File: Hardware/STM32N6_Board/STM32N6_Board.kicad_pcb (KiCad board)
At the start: 2 copper layers, 1 x 0.7 mm, 141 parts, among them J1 Conn_01x02_Pin, J10 BOOT0, J11 Conn_01x18_Socket, J12 Conn_01x18_Socket, J2 Conn_01x02_Pin, J3 Conn_01x08_Pin, J4 Conn_01x18_Pin, J5 Conn_01x18_Pin, J6 Conn_01x05_Pin, J7 SFW15R-2STE1LF, J8 12401832E402A, J9 BOOT1, SW2 SW_Push, U1 STM32N657I0H3Q, U10 STMPS2151STR, U11 IS42S16800F-7BL, U12 ECMF2-40A100N6, U13 ECMF2-40A100N6, U14 ECMF2-40A100N6, U2 SPX5205-ADJ, U3 SPX5205-ADJ, U4 SPX5205-ADJ, U5 SPX5205-ADJ, U6 MC34064-ADJ-TR, U7 MX25LM51245GXDI00, U8 SPX5205-ADJ, U9 ECMF2-40A100N6, Y1 32.768kHz, Y3 48MHz

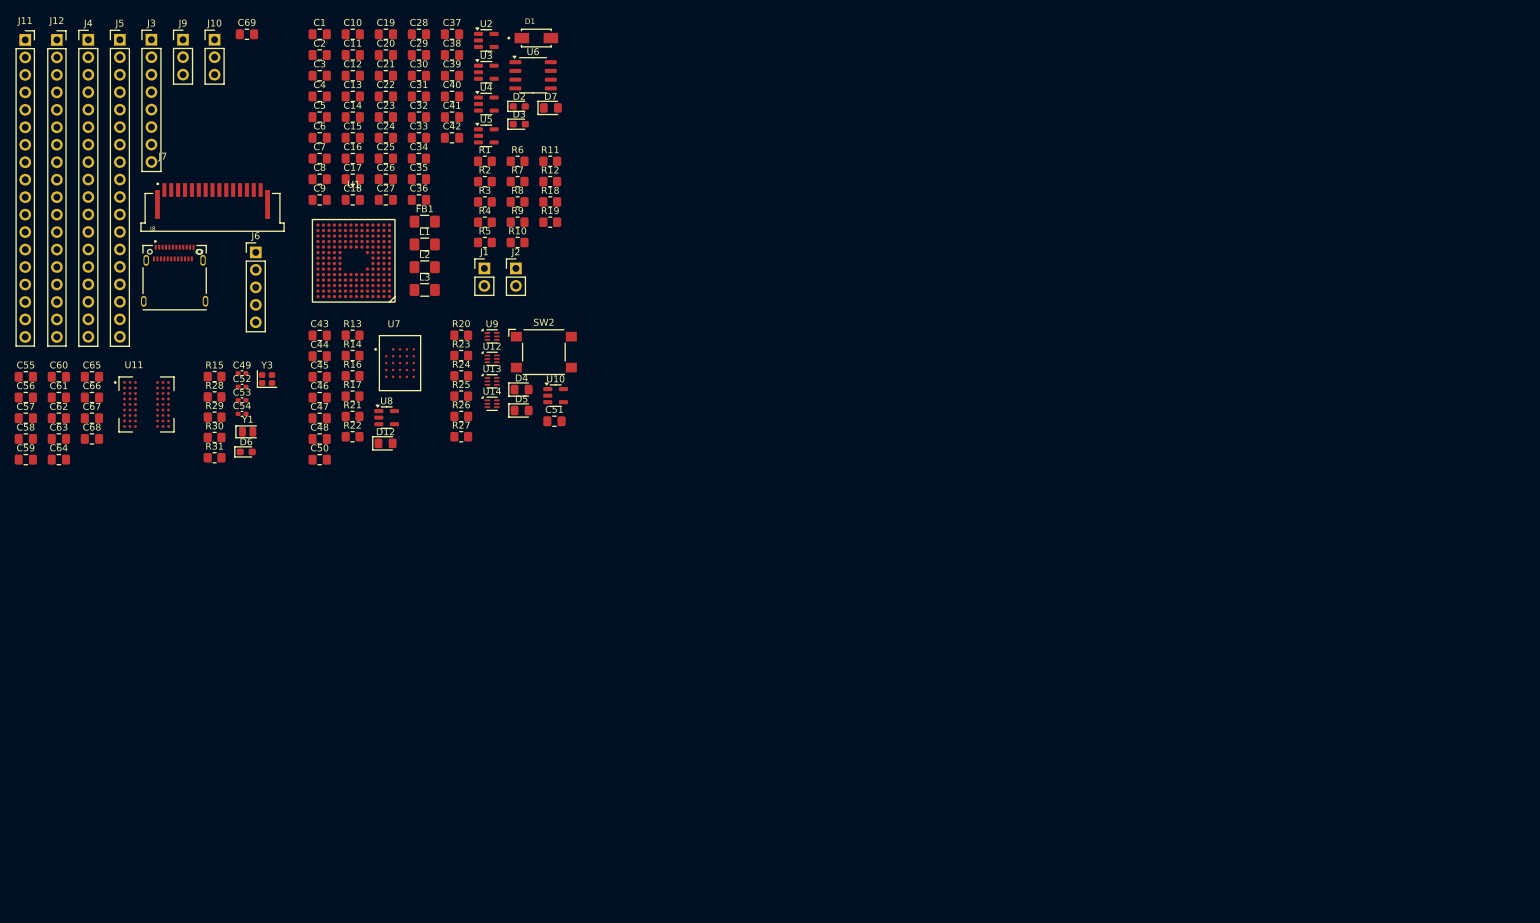
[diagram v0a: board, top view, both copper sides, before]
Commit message: Completed a lot of the layout of the STM Board
- Major layout complete, but all the wiring still left. 488 open nets!
- The STM32's BGA fanout is complete, now comes laying out traces
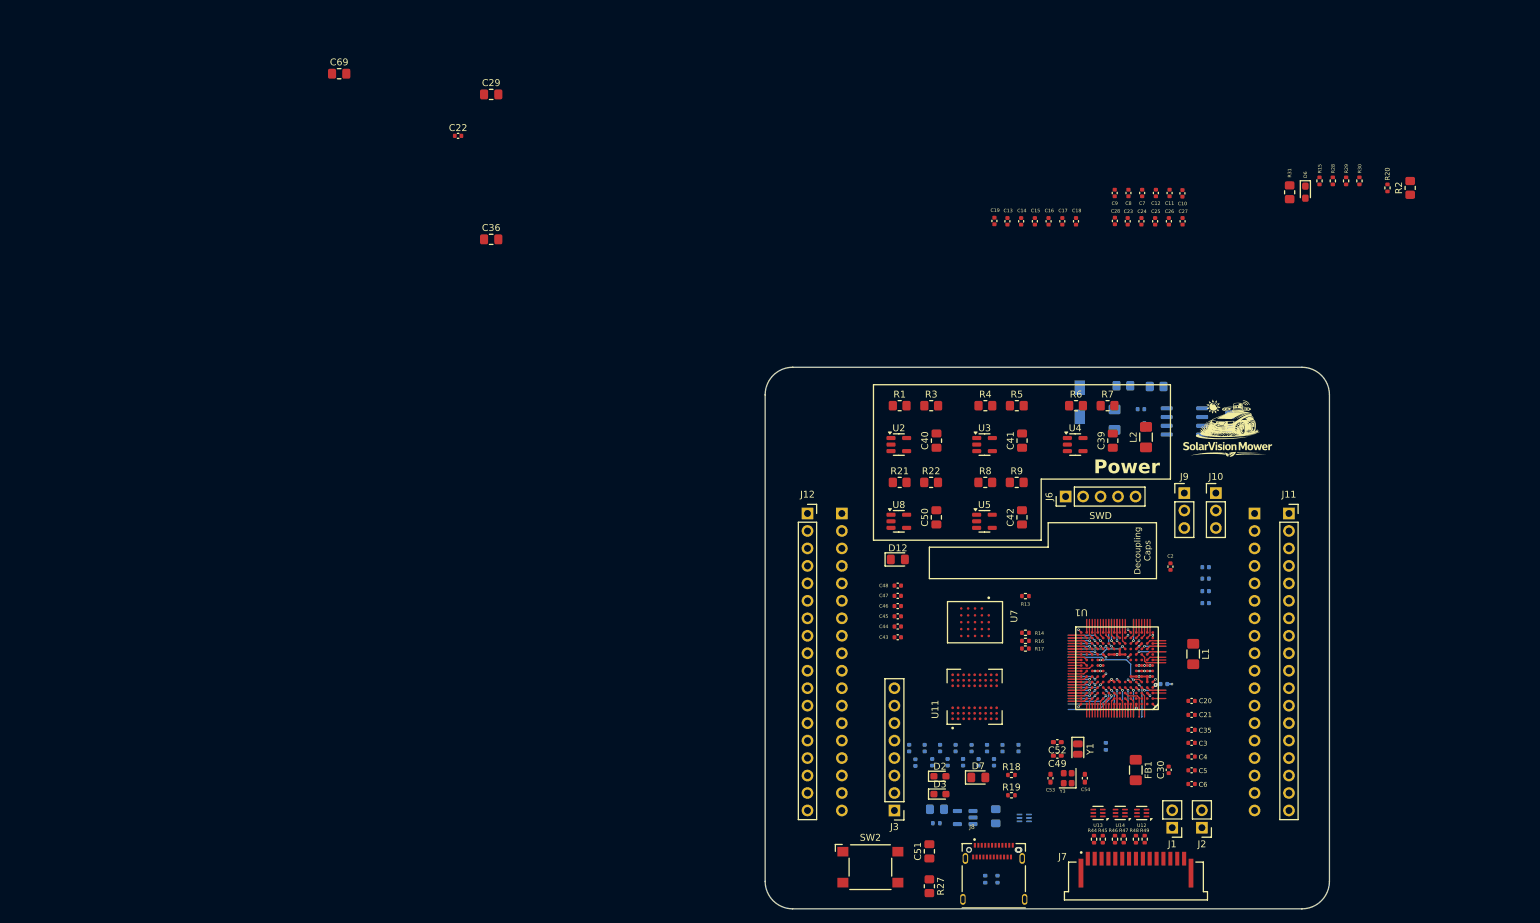
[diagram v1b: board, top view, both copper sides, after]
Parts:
- added G***: LOGO, STM32N6_Footprints:SolarVisionMowerLogo, F.Cu at (216.2, 87.6)
- added R44: 0R, Resistor_SMD:R_0402_1005Metric, F.Cu at (196.7, 147.4)
- added R45: 0R, Resistor_SMD:R_0402_1005Metric, F.Cu at (197.9, 147.4)
- added R46: 0R, Resistor_SMD:R_0402_1005Metric, F.Cu at (199.7, 147.4)
- added R47: 0R, Resistor_SMD:R_0402_1005Metric, F.Cu at (201.0, 147.3)
- added R48: 0R, Resistor_SMD:R_0402_1005Metric, F.Cu at (202.8, 147.4)
- added R49: 0R, Resistor_SMD:R_0402_1005Metric, F.Cu at (204.0, 147.3)
- C1, C31, C32, C33, C34, C37, C38, C55, C56, C57, C58, C59, C60, C61, C62, C63, C64, C65, C66, C67, C68: footprint Capacitor_SMD:C_0805_2012Metric_Pad1.18x1.45mm_HandSolder -> Capacitor_SMD:C_0402_1005Metric; moved to B.Cu
- C10, C11, C12, C13, C14, C15, C16, C17, C18, C19, C2, C20, C21, C22, C23, C24, C25, C26, C27, C28, C3, C30, C35, C4, C43, C44, C45, C46, C47, C48, C5, C6, C7, C8, C9: footprint Capacitor_SMD:C_0805_2012Metric_Pad1.18x1.45mm_HandSolder -> Capacitor_SMD:C_0402_1005Metric
- D1, D4, D5, J4, J5, L3, R10, R11, R12, U10, U6, U9: moved to B.Cu
- R13, R14, R15, R16, R17, R18, R19, R20, R28, R29, R30: footprint Resistor_SMD:R_0805_2012Metric_Pad1.20x1.40mm_HandSolder -> Resistor_SMD:R_0402_1005Metric
- R23, R24, R25, R26: footprint Resistor_SMD:R_0805_2012Metric_Pad1.20x1.40mm_HandSolder -> Resistor_SMD:R_0402_1005Metric; moved to B.Cu
- moved J11 196.2 mm to (225.0, 100.0)
- moved J4 183.0 mm to (220.0, 100.0), turned to 180 degrees
- moved R30 170.6 mm to (235.2, 51.6), turned to 90 degrees
- moved R29 168.1 mm to (233.3, 51.6), turned to 90 degrees
- moved J7 165.8 mm to (202.8, 152.3)
- moved R28 165.6 mm to (231.4, 51.6), turned to 90 degrees
- moved R15 163.1 mm to (229.4, 51.6), turned to 90 degrees
- moved R31 161.0 mm to (225.1, 53.3), turned to -90 degrees
- moved J10 159.8 mm to (214.4, 97.0)
- moved J9 159.8 mm to (209.8, 97.0)
- moved C3 159.6 mm to (210.8, 133.3)
- moved C4 159.0 mm to (210.8, 135.3)
- moved D6 158.6 mm to (227.4, 53.3), turned to -90 degrees
- moved C5 158.4 mm to (210.8, 137.3)
- moved C6 157.8 mm to (210.8, 139.3)
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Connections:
- net Net-(U6-DRC) renamed /Power_Unit/Buck_Feedback
- C35 pad 2: /Power_Unit/VFBSMPS -> GND
- J7 pad 2: /Analog_Unit/D0N -> Net-(J7-Pad2)
- J7 pad 3: /Analog_Unit/D0P -> Net-(J7-Pad3)
- J7 pad 5: /Analog_Unit/D1N -> Net-(J7-Pad5)
- J7 pad 6: /Analog_Unit/D1P -> Net-(J7-Pad6)
- J7 pad 8: /Analog_Unit/CKN -> Net-(J7-Pad8)
- J7 pad 9: /Analog_Unit/CKP -> Net-(J7-Pad9)
- U1 pad N11: /Analog_Unit/EN -> /Analog_Unit/EN_USB
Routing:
- net /Analog_Unit/PWR_ON: track 0.00 -> 13.4 mm, vias 0 -> 1
- net GND: track 0.00 -> 10.3 mm, vias 0 -> 12
- net /FMC_SDRAM/FMC_D0: track 0.00 -> 8.96 mm, vias 0 -> 1
- net /FMC_SDRAM/FMC_SDNRAS: track 0.00 -> 8.04 mm, vias 0 -> 1
- net /FMC_SDRAM/FMC_SDNE0: track 0.00 -> 7.82 mm, vias 0 -> 1
- net /FMC_SDRAM/FMC_SKNCAS: track 0.00 -> 6.40 mm, vias 0 -> 1
- net /FMC_SDRAM/FMC_D6: track 0.00 -> 6.24 mm, vias 0 -> 1
- net /FMC_SDRAM/FMC_D9: track 0.00 -> 5.60 mm, vias 0 -> 1
- net /Analog_Unit/NRST: track 0.00 -> 5.45 mm, vias 0 -> 1
- net /FMC_SDRAM/FMC_A0: track 0.00 -> 5.43 mm, vias 0 -> 1
- net /Connectors/HDP0: track 0.00 -> 5.13 mm
- net /FMC_SDRAM/FMC_A5: track 0.00 -> 4.63 mm, vias 0 -> 1
- net /FMC_SDRAM/FMC_A3: track 0.00 -> 4.63 mm, vias 0 -> 1
- net /Connectors/SPI1_MOSI: track 0.00 -> 4.63 mm, vias 0 -> 1
- net /FMC_SDRAM/FMC_A4: track 0.00 -> 4.63 mm, vias 0 -> 1
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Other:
- board size 1 x 0.7 mm -> 82 x 78.7 mm
- copper layers 2 -> 4
- board text added: "Decoupling Caps"
- board text added: "Power"
- board text added: "SWD"

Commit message: Added bypass capacitors to the STM32
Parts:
- C10, C11, C12, C13, C14, C15, C16, C17, C18, C19, C23, C24, C25, C26, C27, C28, C3, C35, C4, C5, C6, C7, C8, C9: moved to B.Cu
- R2: footprint Resistor_SMD:R_0805_2012Metric_Pad1.20x1.40mm_HandSolder -> Resistor_SMD:R_0402_1005Metric
- moved R2 72.7 mm to (213.7, 119.4), turned to -90 degrees
- moved C9 70.0 mm to (207.5, 122.9)
- moved C12 69.7 mm to (210.6, 122.9)
- moved C8 69.7 mm to (206.5, 122.9)
- moved C11 69.6 mm to (209.6, 122.9)
- moved C7 69.6 mm to (205.5, 122.9)
- moved C10 69.5 mm to (208.5, 122.9)
- moved C17 68.0 mm to (200.7, 125.0), turned to 0 degrees
- moved C18 67.6 mm to (198.7, 125.0), turned to 180 degrees
- moved C19 67.3 mm to (198.9, 122.7), turned to -90 degrees
- moved C13 67.0 mm to (199.9, 122.7), turned to -90 degrees
- moved C14 65.3 mm to (196.8, 121.9)
- moved C15 64.9 mm to (195.8, 121.9)
- moved C16 64.6 mm to (194.8, 121.9)
- moved C28 62.3 mm to (202.4, 119.7)
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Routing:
- net GND: track 10.3 -> 39.4 mm, vias 12 -> 21
- net /Power_Unit/VFBSMPS: track 2.87 -> 14.8 mm, vias 0 -> 1
- net /Power_Unit/VLXSMPS: track 2.40 -> 14.2 mm
- net VDD: track 4.10 -> 11.7 mm
- net /Power_Unit/VDDCORE: track 3.77 -> 11.2 mm
- net /Power_Unit/VDDSMPS: track 2.40 -> 8.31 mm, vias 3 -> 5
- net /Power_Unit/VREFP: track 1.90 -> 7.38 mm
- net /Connectors/USART3_RX: track 3.67 -> 8.67 mm
- net /Connectors/SPI1_MISO: track 4.63 -> 9.63 mm
- net /Connectors/I2C1_SCL: track 4.63 -> 9.63 mm
- net /Connectors/USART3_TX: track 2.87 -> 7.87 mm
- net /Connectors/USART2_TX: track 1.90 -> 6.90 mm
- net /Connectors/USART2_RX: track 2.87 -> 7.87 mm
- net /Connectors/USART1_TX: track 2.87 -> 7.87 mm
- net /Connectors/USART1_RX: track 3.67 -> 8.67 mm
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- added copper zone on In2.Cu, net +5V
- added copper zone on In1.Cu, net GND
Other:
- board text removed: "Decoupling Caps"

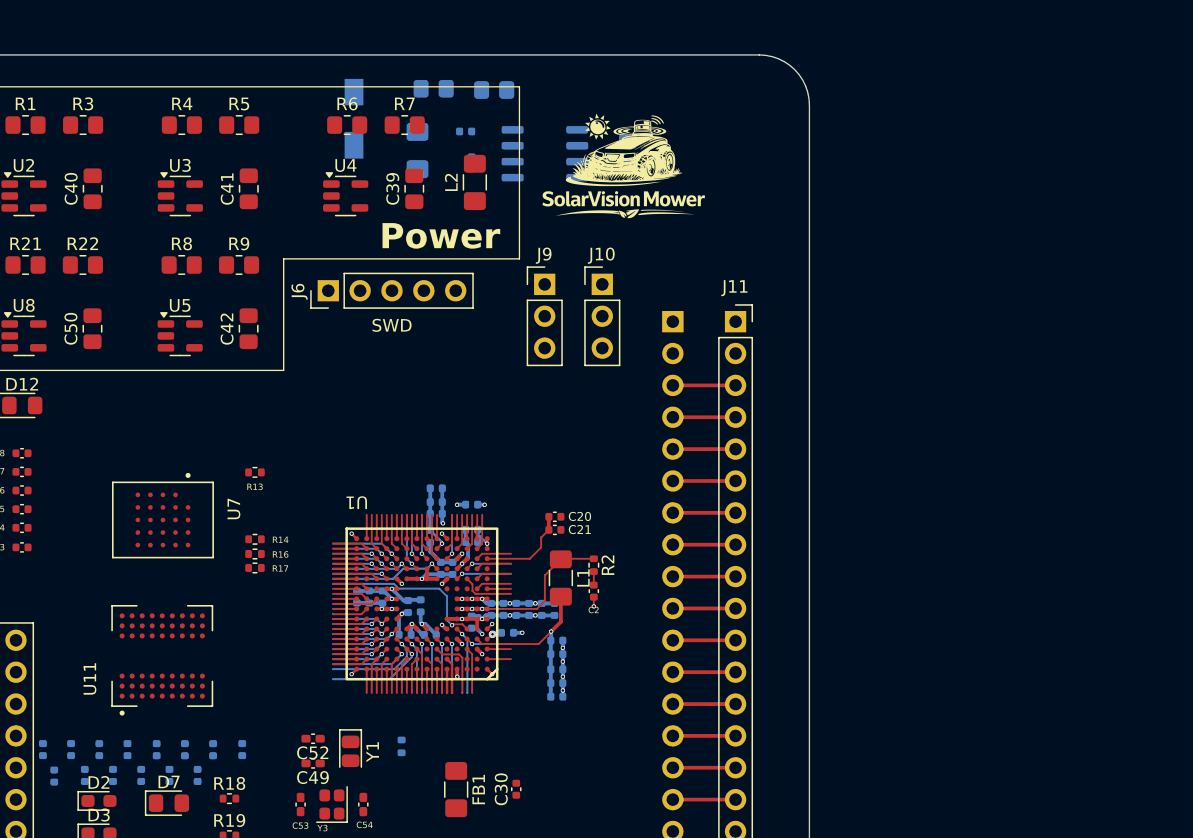
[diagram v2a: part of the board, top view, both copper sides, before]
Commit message: Completed SDRAM bga fanout
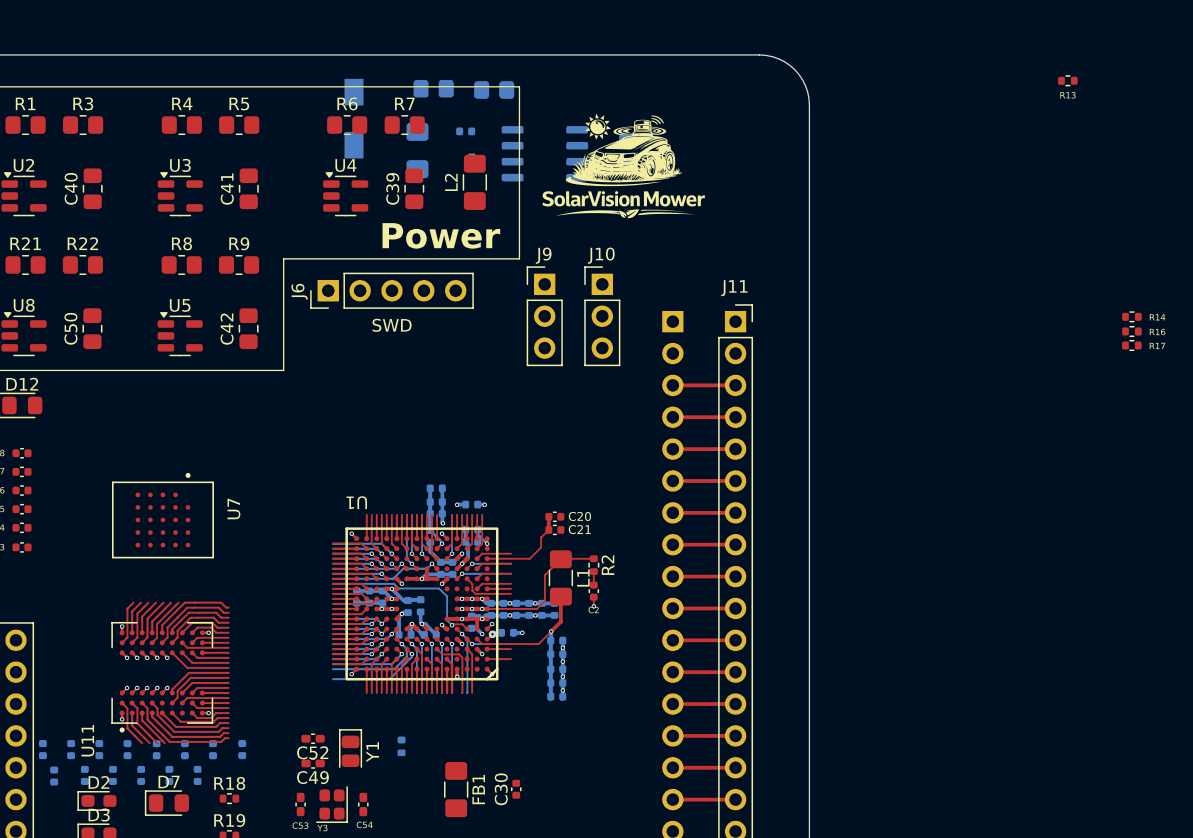
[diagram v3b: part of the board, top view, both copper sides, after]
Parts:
- moved R14 72.1 mm to (256.6, 99.6)
- moved R16 72.1 mm to (256.6, 100.8)
- moved R17 72.1 mm to (256.6, 101.9)
- moved R13 71.9 mm to (251.5, 80.8)
- moved U11 1.35 mm to (179.3, 128.0)
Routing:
- net /FMC_SDRAM/FMC_D11: track 1.90 -> 10.7 mm
- net /FMC_SDRAM/FMC_D9: track 5.60 -> 13.1 mm
- net /FMC_SDRAM/FMC_D10: track 2.87 -> 10.1 mm
- net /FMC_SDRAM/FMC_NBL0: track 2.87 -> 9.96 mm
- net /FMC_SDRAM/FMC_D7: track 1.90 -> 8.71 mm
- net /FMC_SDRAM/FMC_D8: track 4.63 -> 10.5 mm
- net /FMC_SDRAM/FMC_SDNRAS: track 8.04 -> 13.8 mm
- net /FMC_SDRAM/FMC_SDCLK: track 3.67 -> 9.31 mm
- net /FMC_SDRAM/FMC_SDNWE: track 2.87 -> 8.36 mm
- net /FMC_SDRAM/FMC_SDCKE0: track 2.87 -> 8.19 mm
- net /FMC_SDRAM/FMC_SKNCAS: track 6.40 -> 11.4 mm
- net /FMC_SDRAM/FMC_NBL1: track 3.67 -> 8.57 mm
- net /FMC_SDRAM/FMC_SDNE0: track 7.82 -> 12.0 mm
- net /FMC_SDRAM/FMC_D6: track 6.24 -> 10.3 mm
- net /FMC_SDRAM/FMC_BA0: track 1.90 -> 5.93 mm
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
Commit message: Completed the IS42S SDRAM routing. Lord have mercy
- Routing is complete (somewhat)
- Spacing between traces is 0.5mm, address and data lines 0.1565mm wide
- 0.1565mm should maintain ~50 Ohms impedance.
- STILL NEED TO DO:
  - Length matching. Datasheet + STM App Note says +-10mm
  - 10nF stitching caps along vias, for return currents
- Remind me to *never* use a 4-layer board for something like this
  again. D:
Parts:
- moved C59 66.5 mm to (246.4, 119.3)
- moved C66 66.5 mm to (247.7, 117.2)
- moved C57 66.5 mm to (242.0, 119.3)
- moved C58 66.5 mm to (244.2, 119.3)
- moved C67 66.5 mm to (245.4, 117.2)
- moved C68 66.5 mm to (243.2, 117.2)
- moved C49 60.5 mm to (251.8, 134.1)
- moved C52 60.5 mm to (251.8, 132.1)
- moved Y1 60.5 mm to (254.8, 133.1)
- moved C65 4.45 mm to (187.8, 138.0)
- moved U7 4.05 mm to (176.9, 112.6)
- moved U11 2.47 mm to (176.8, 128.0)
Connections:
- U11 pad A2: /FMC_SDRAM/FMC_D15 -> /FMC_SDRAM/FMC_D10
- U11 pad A8: /FMC_SDRAM/FMC_D0 -> /FMC_SDRAM/FMC_D1
- U11 pad B1: /FMC_SDRAM/FMC_D14 -> /FMC_SDRAM/FMC_D11
- U11 pad B2: /FMC_SDRAM/FMC_D13 -> /FMC_SDRAM/FMC_D8
- U11 pad B8: /FMC_SDRAM/FMC_D2 -> /FMC_SDRAM/FMC_D4
- U11 pad B9: /FMC_SDRAM/FMC_D1 -> /FMC_SDRAM/FMC_D3
- U11 pad C2: /FMC_SDRAM/FMC_D11 -> /FMC_SDRAM/FMC_D13
- U11 pad C8: /FMC_SDRAM/FMC_D4 -> /FMC_SDRAM/FMC_D7
- U11 pad C9: /FMC_SDRAM/FMC_D3 -> /FMC_SDRAM/FMC_D5
- U11 pad D1: /FMC_SDRAM/FMC_D10 -> /FMC_SDRAM/FMC_D14
- U11 pad D2: /FMC_SDRAM/FMC_D9 -> /FMC_SDRAM/FMC_D15
- U11 pad D8: /FMC_SDRAM/FMC_D6 -> /FMC_SDRAM/FMC_D0
- U11 pad D9: /FMC_SDRAM/FMC_D5 -> /FMC_SDRAM/FMC_D6
- U11 pad E1: /FMC_SDRAM/FMC_D8 -> /FMC_SDRAM/FMC_D9
- U11 pad E9: /FMC_SDRAM/FMC_D7 -> /FMC_SDRAM/FMC_D2
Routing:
- net /FMC_SDRAM/FMC_D1: track 6.36 -> 42.7 mm
- net /FMC_SDRAM/FMC_D3: track 6.52 -> 40.0 mm, vias 1 -> 2
- net /FMC_SDRAM/FMC_D4: track 5.80 -> 37.7 mm
- net /FMC_SDRAM/FMC_D5: track 5.89 -> 36.3 mm
- net /FMC_SDRAM/FMC_A10: track 5.14 -> 34.8 mm, vias 0 -> 4
- net /FMC_SDRAM/FMC_A1: track 4.97 -> 33.3 mm, vias 0 -> 4
- net /FMC_SDRAM/FMC_D12: track 6.03 -> 33.4 mm, vias 0 -> 2
- net /FMC_SDRAM/FMC_D10: track 10.1 -> 37.3 mm, vias 0 -> 2
- net /FMC_SDRAM/FMC_A2: track 4.97 -> 31.8 mm, vias 0 -> 4
- net /FMC_SDRAM/FMC_D8: track 10.5 -> 37.1 mm, vias 1 -> 4
- net /FMC_SDRAM/FMC_D13: track 5.93 -> 32.5 mm, vias 0 -> 2
- net /FMC_SDRAM/FMC_D14: track 4.88 -> 31.2 mm, vias 0 -> 2
- net /FMC_SDRAM/FMC_SDNWE: track 8.36 -> 34.4 mm, vias 0 -> 2
- net /FMC_SDRAM/FMC_D15: track 6.73 -> 32.1 mm, vias 0 -> 2
- net /FMC_SDRAM/FMC_D7: track 8.71 -> 34.1 mm
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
